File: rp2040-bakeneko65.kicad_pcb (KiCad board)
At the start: 2 copper layers, 303.8 x 94.2 mm, 200 parts, among them J1 SM04B-SRSS-TB, J2 SWD, SW1 1u, SW10 1u, SW11 1u, SW12 1u, SW13 1u, SW14 1u, SW15 1u, SW16 1u, SW17 2u, SW18 1.5u, SW19 1u, SW2 1u, SW20 1u, SW21 1u, SW22 1u, SW23 1u, SW24 1u, SW25 1u, SW26 1u, SW27 1u, SW28 1u, SW29 1u, SW3 1u, SW30 1u, SW31 1.5u, SW32 ISO Enter, SW33 1u, SW34 1.25u, SW35 1.75u, SW36 1u, SW37 1u, SW38 1u, SW39 1u, SW4 1u, SW40 1u, SW41 1u, SW42 1u, SW43 1u, SW44 1u, SW45 1u, SW46 1u, SW47 2.25u, SW48 1u, SW49 1u, SW5 1u, SW50 2.25u, SW51 1.25u, SW52 1u, SW53 1u, SW54 1u, SW55 1u, SW56 1u, SW57 1u, SW58 1u, SW59 1u, SW6 1u, SW60 1u, SW61 1u, SW62 1u, SW63 1.75u, SW64 1u, SW65 1u, SW66 1.5u, SW67 1.25u, SW68 1u, SW69 1.25u, SW7 1u, SW70 1.5u, SW71 1.25u, SW72 3u, SW73 2.25u, SW74 7u, SW75 6.25u, SW76 2u, SW77 3u, SW78 2.75u, SW79 1.25u, SW8 1u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

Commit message: Some extra routing
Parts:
- S32: footprint marbastlib-mx:STAB_MX_ISO -> marbastlib-mx:STAB_MX_P_ISO
- moved SW85 34.3 mm to (73.5, 118.8), turned to -90 degrees
- turned S32 to 180 degrees
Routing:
- net COL13: track 0.00 -> 111.5 mm
- net COL15: track 5.41 -> 82.6 mm
- net COL14: track 0.00 -> 9.57 mm
- net GND: vias 2 -> 11

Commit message: actually place encoder correctly
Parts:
- moved SW85 622.7 mm to (25.8, 116.2), turned to 90 degrees
- moved R3 513.7 mm to (27.6, 105.5), turned to -90 degrees
- moved J2 443.1 mm to (74.2, 140.7), turned to 90 degrees
- moved F1 191.3 mm to (515.6, 121.8)
- moved R3 39.0 mm to (82.0, 125.1), turned to -90 degrees
- moved D77 4.28 mm to (251.2, 171.4)
- moved D46 1.44 mm to (300.5, 134.4)
- moved SW85 1.21 mm to (74.5, 119.5)
- moved SW86 0.11 mm to (352.3, 100.2)
- turned S72 to 180 degrees
- turned S73 to 180 degrees
- turned S74 to 180 degrees
- turned S75 to 180 degrees
- turned S76 to 180 degrees
- turned S77 to 180 degrees
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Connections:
- SW86 pad S1: ROW0 -> Net-(D16-A)
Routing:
- net RESET: track 0.36 -> 31.2 mm
- net GND: track 6.99 -> 15.9 mm, vias 11 -> 12
- net COL15: track 82.6 -> 83.5 mm

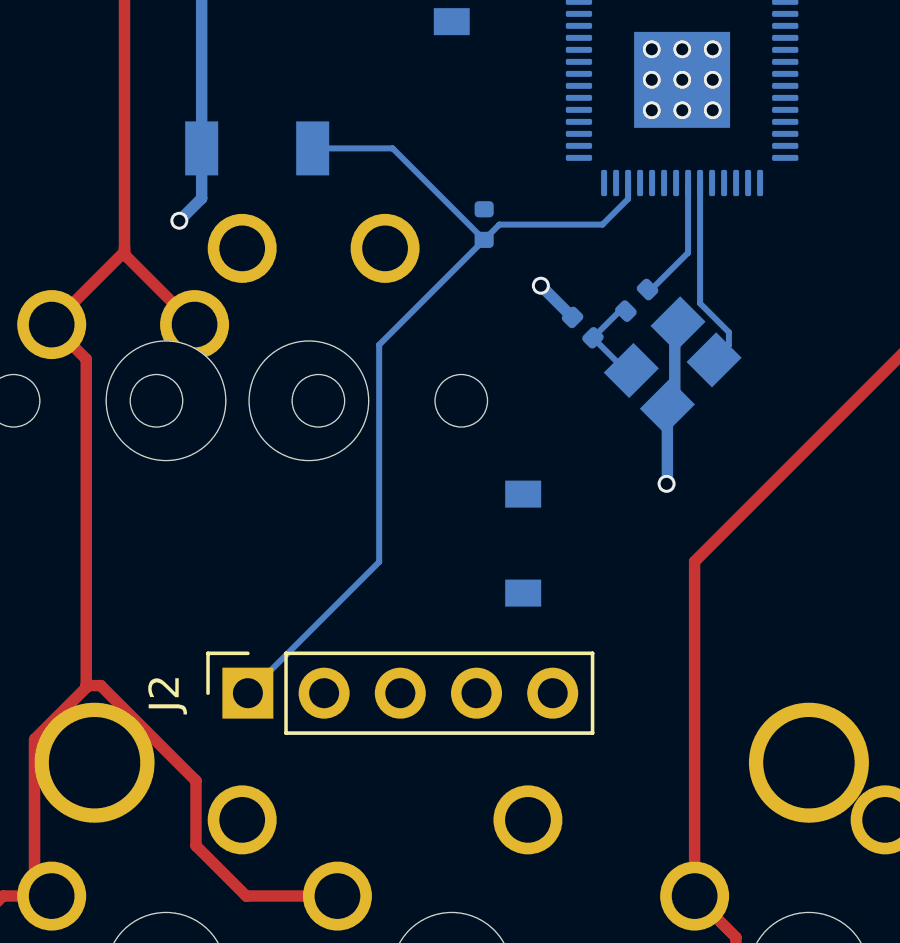
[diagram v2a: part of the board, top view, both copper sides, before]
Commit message: Route debug header
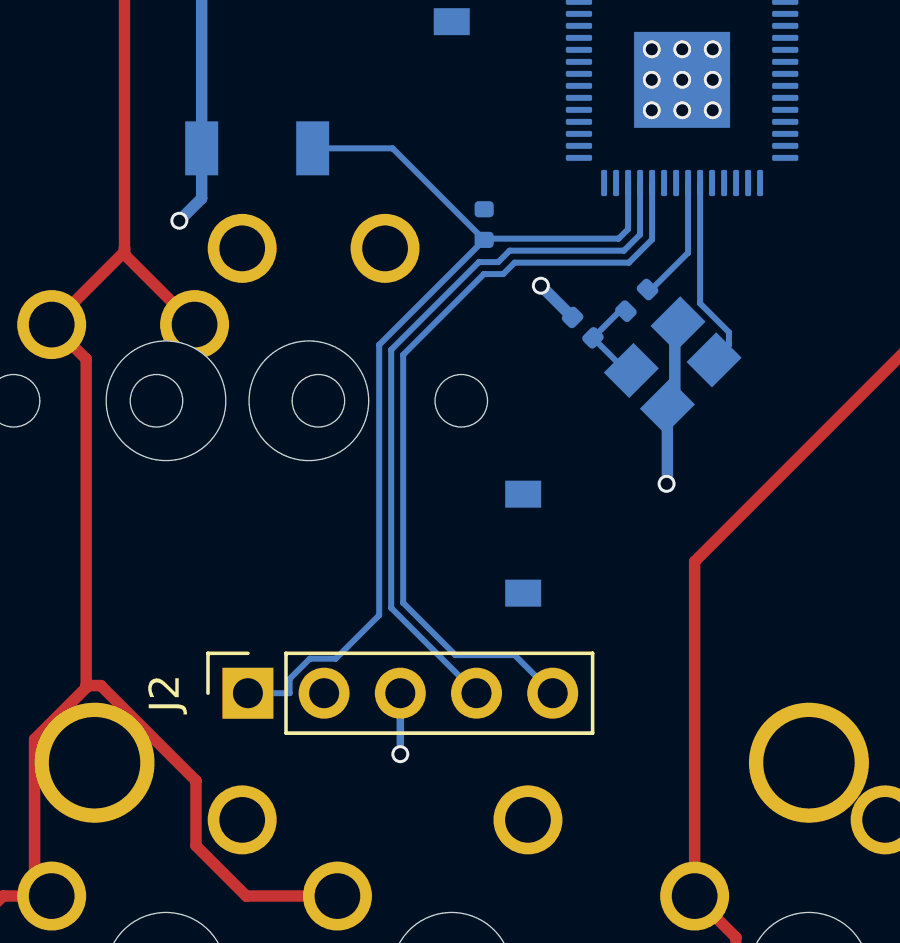
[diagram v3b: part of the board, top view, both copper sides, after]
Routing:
- net SWCLK: track 0.00 -> 26.3 mm
- net SWD: track 0.00 -> 24.2 mm
- net GND: track 15.9 -> 17.9 mm, vias 12 -> 13
- net RESET: track 31.2 -> 33.2 mm

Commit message: A couple decoupling caps
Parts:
- moved C11 448.3 mm to (86.7, 127.5), turned to -135 degrees
- moved C7 428.7 mm to (85.9, 126.7), turned to -135 degrees
- moved C3 3.32 mm to (88.6, 128.2)
- moved R4 3.32 mm to (90.4, 127.3)
- moved Y1 3.32 mm to (91.6, 129.4)
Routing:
- net +3V3: track 0.00 -> 4.02 mm
- net +1V1: track 0.00 -> 3.73 mm
- net RESET: track 33.2 -> 31.2 mm
- net XTAL_IN: track 6.50 -> 8.06 mm

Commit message: (poorly) route JST
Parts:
- moved R2 457.3 mm to (86.6, 113.2), turned to -90 degrees
- moved R1 450.4 mm to (87.6, 113.2), turned to -90 degrees
- moved U2 443.4 mm to (86.5, 102.1), turned to -90 degrees
- moved U4 418.3 mm to (114.6, 103.5), turned to 90 degrees
- moved F1 396.7 mm to (119.8, 96.8), turned to 0 degrees
- moved J1 394.3 mm to (126.0, 100.2), turned to -90 degrees
- moved D72 6.25 mm to (170.6, 173.9)
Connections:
- R1 pad 1: D+ -> /D_P
- R2 pad 1: D- -> /D_N
- U4 pad 3: D- -> /D_P
- U4 pad 4: unconnected-(U4-IO3-Pad4) -> /D_N
- U4 pad 6: unconnected-(U4-IO4-Pad6) -> D-
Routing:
- net /D_N: track 0.00 -> 34.7 mm
- net /D_P: track 0.00 -> 33.5 mm
- net D+: track 0.00 -> 10.3 mm
- net D-: track 0.00 -> 9.55 mm
- net +5V: track 0.00 -> 7.14 mm
- net Net-(J1-Pin_1): track 0.00 -> 3.66 mm
- net GND: track 17.5 -> 19.6 mm, vias 13 -> 14

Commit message: Add voltage regulator
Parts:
- moved U3 447.7 mm to (100.8, 101.8), turned to 0 degrees
- moved U2 3.00 mm to (83.5, 102.3), turned to 90 degrees
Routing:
- net +5V: track 7.14 -> 28.6 mm
- net GND: track 19.6 -> 22.8 mm, vias 14 -> 15

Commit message: get started on flash
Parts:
- moved U2 24.0 mm to (101.0, 118.7), turned to 0 degrees
- moved D19 6.84 mm to (106.2, 110.0)
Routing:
- net GND: track 22.8 -> 13.9 mm, vias 15 -> 14
- net SD2: track 0.00 -> 8.91 mm
- net SD1: track 0.00 -> 8.50 mm
- net CS: track 0.00 -> 7.71 mm
- net RESET: track 31.2 -> 24.3 mm

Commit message: flash, redo ESD, some other stuff
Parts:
- U4: value SRV05-4 -> SRV05
- moved C13 449.5 mm to (88.6, 113.2), turned to 90 degrees
- moved C12 441.1 mm to (93.9, 117.7), turned to -45 degrees
- moved C8 424.6 mm to (89.7, 113.2), turned to 90 degrees
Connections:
- R1 pad 1: /D_P -> D+
- R2 pad 1: /D_N -> D-
- U4 pad 3: /D_P -> unconnected-(U4-IO2-Pad3)
- U4 pad 4: /D_N -> unconnected-(U4-IO3-Pad4)
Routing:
- net D-: track 9.55 -> 43.2 mm
- net D+: track 10.3 -> 43.0 mm
- net /D_N: track 34.7 -> 3.42 mm
- net /D_P: track 33.5 -> 3.17 mm
- net SD3: track 0.00 -> 23.4 mm
- net QSPI_CLK: track 0.00 -> 20.4 mm
- net SD0: track 0.00 -> 16.5 mm
- net +3V3: track 4.02 -> 12.3 mm
- net GND: track 13.9 -> 19.1 mm, vias 14 -> 17
- net +1V1: track 3.73 -> 7.27 mm
- net CS: track 7.71 -> 9.30 mm
- net SD1: track 8.50 -> 9.02 mm
